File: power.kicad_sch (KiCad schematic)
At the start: 14 parts, among them J11 CON-SOCJ-2155, J12 Header for power lead to QMTE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, J15 696101000002 Fuse Holder 20mm, SW2 SW_SPDT_with_shield, U15 LM2678T-5.0

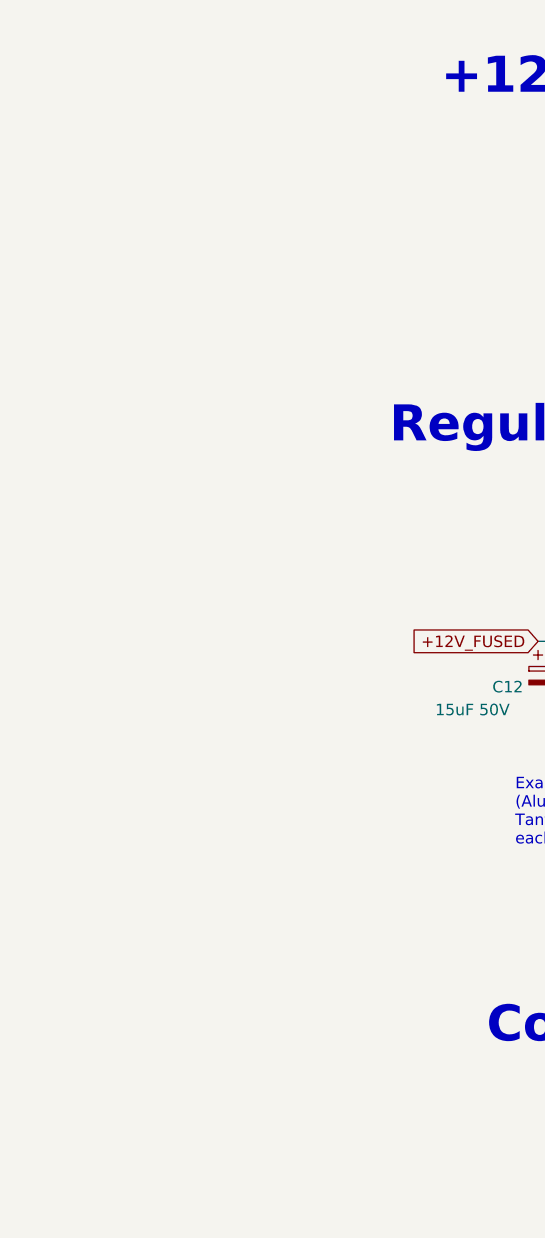
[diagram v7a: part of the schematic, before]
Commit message: place some mounting holes and reset button #3
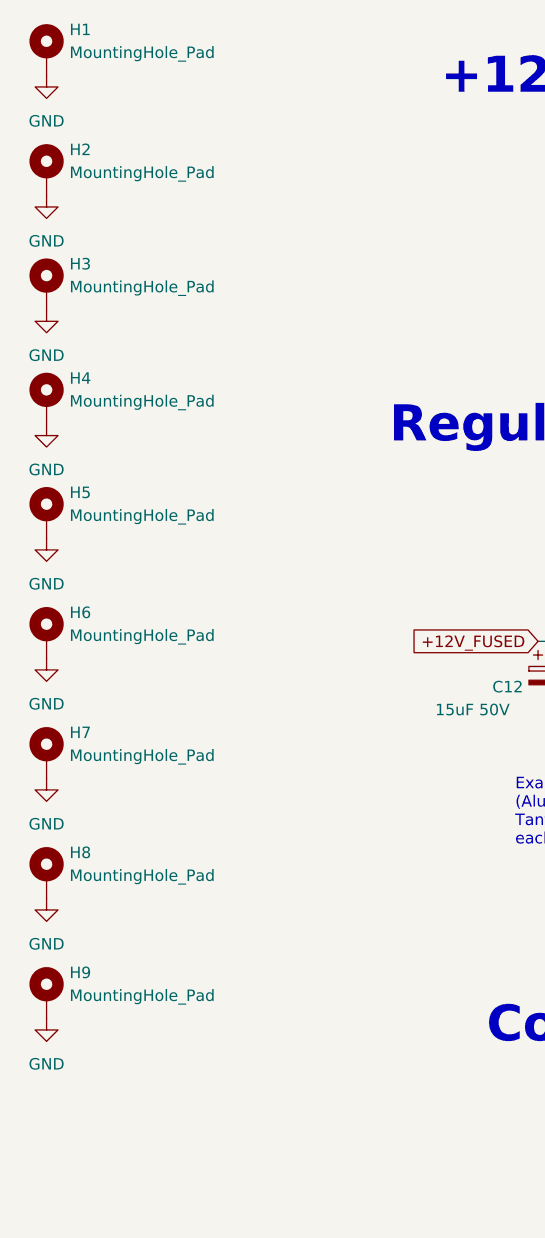
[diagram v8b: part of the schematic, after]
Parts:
- added H1, H2, H3, H4, H5, H6, H7, H8, H9: MountingHole_Pad, MountingHole:MountingHole_3.2mm_M3_DIN965_Pad, symbol Mechanical:MountingHole_Pad
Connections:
- net GND: now also H1.1, H2.1, H3.1, H4.1, H5.1, H6.1, H7.1, H8.1, H9.1
